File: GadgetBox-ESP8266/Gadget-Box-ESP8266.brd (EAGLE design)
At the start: 93.5 x 53.5 mm, 33 parts, among them U1 MCP73831T-2ACI/OT, U2 AP2112-3.3

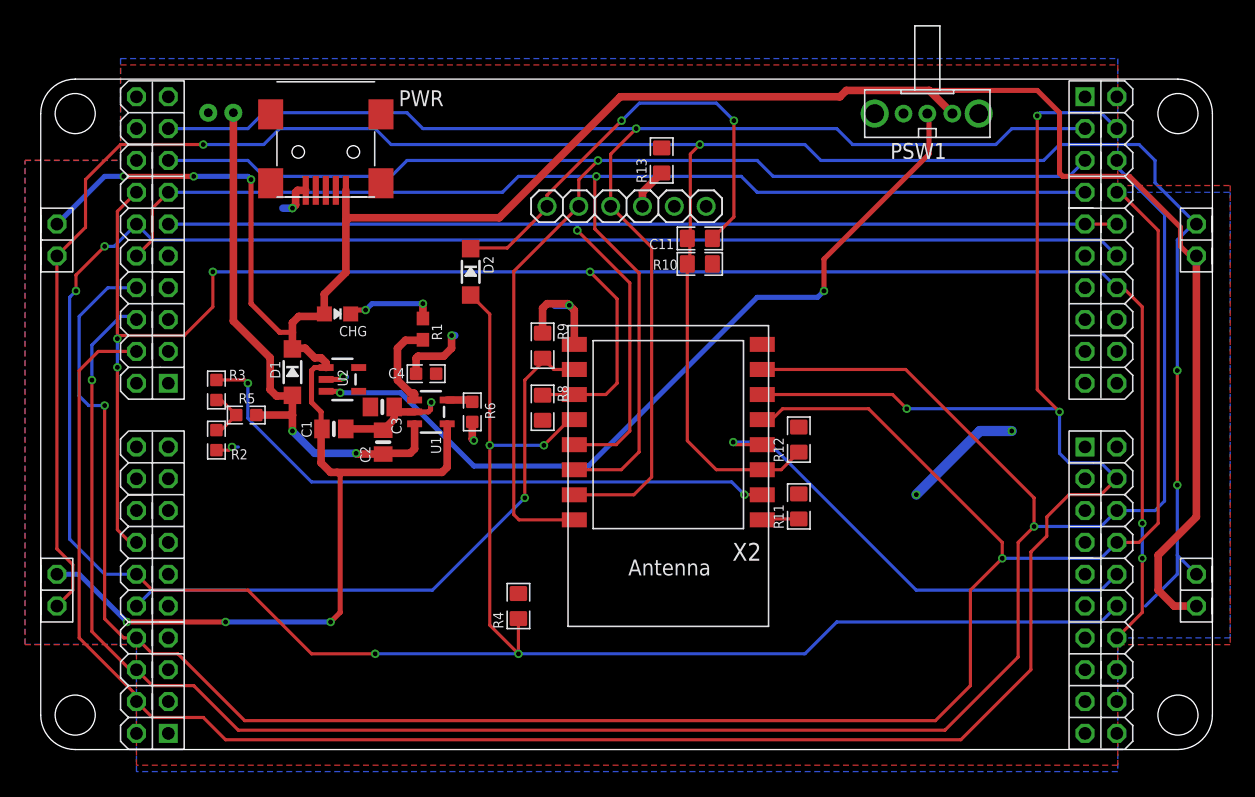
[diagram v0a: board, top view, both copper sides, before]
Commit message: Updated silkscreen and BOM for GadgetBox-ESP8266
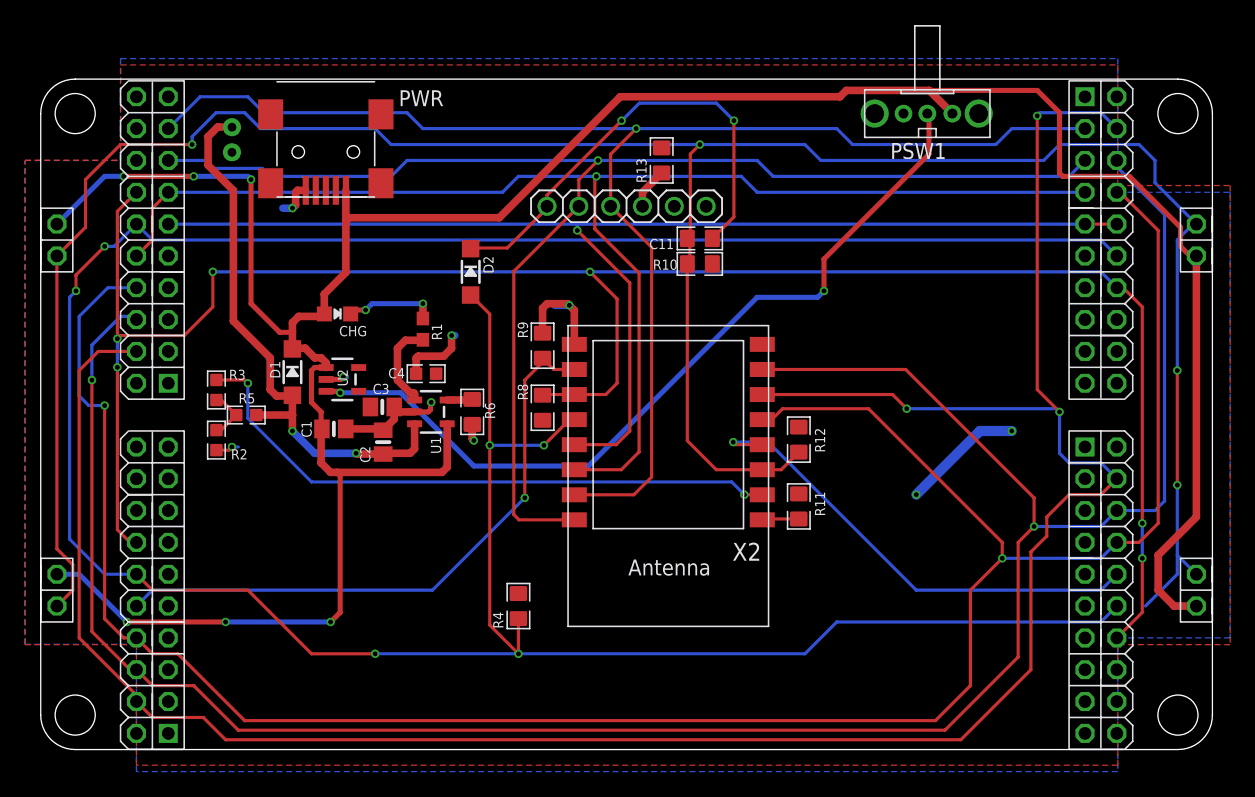
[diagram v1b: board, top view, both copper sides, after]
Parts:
- R6: device GadgetFactory:0603 -> GadgetFactory:0805
- moved JP1 2.33 mm to (16.5, 49.9), turned to 90 degrees
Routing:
- net RESET: track 200.7 -> 202.2 mm
- net VBAT: track 43.7 -> 44.9 mm
- net D0/RX/MISO: track 112.0 -> 113.1 mm
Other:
- board text added: "Gadget Box - ESP8266 Copyright 2016 Gadget Factory, LLC Version 1.1"
- board text removed: "Gadget Box - ESP8266 Copyright 2016 Gadget Factory, LLC Version 1.0"
